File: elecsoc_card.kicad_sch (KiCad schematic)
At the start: 30 parts, among them J1 Conn_01x02_Pin, J2 Conn_01x02_Pin, U1 NA555D

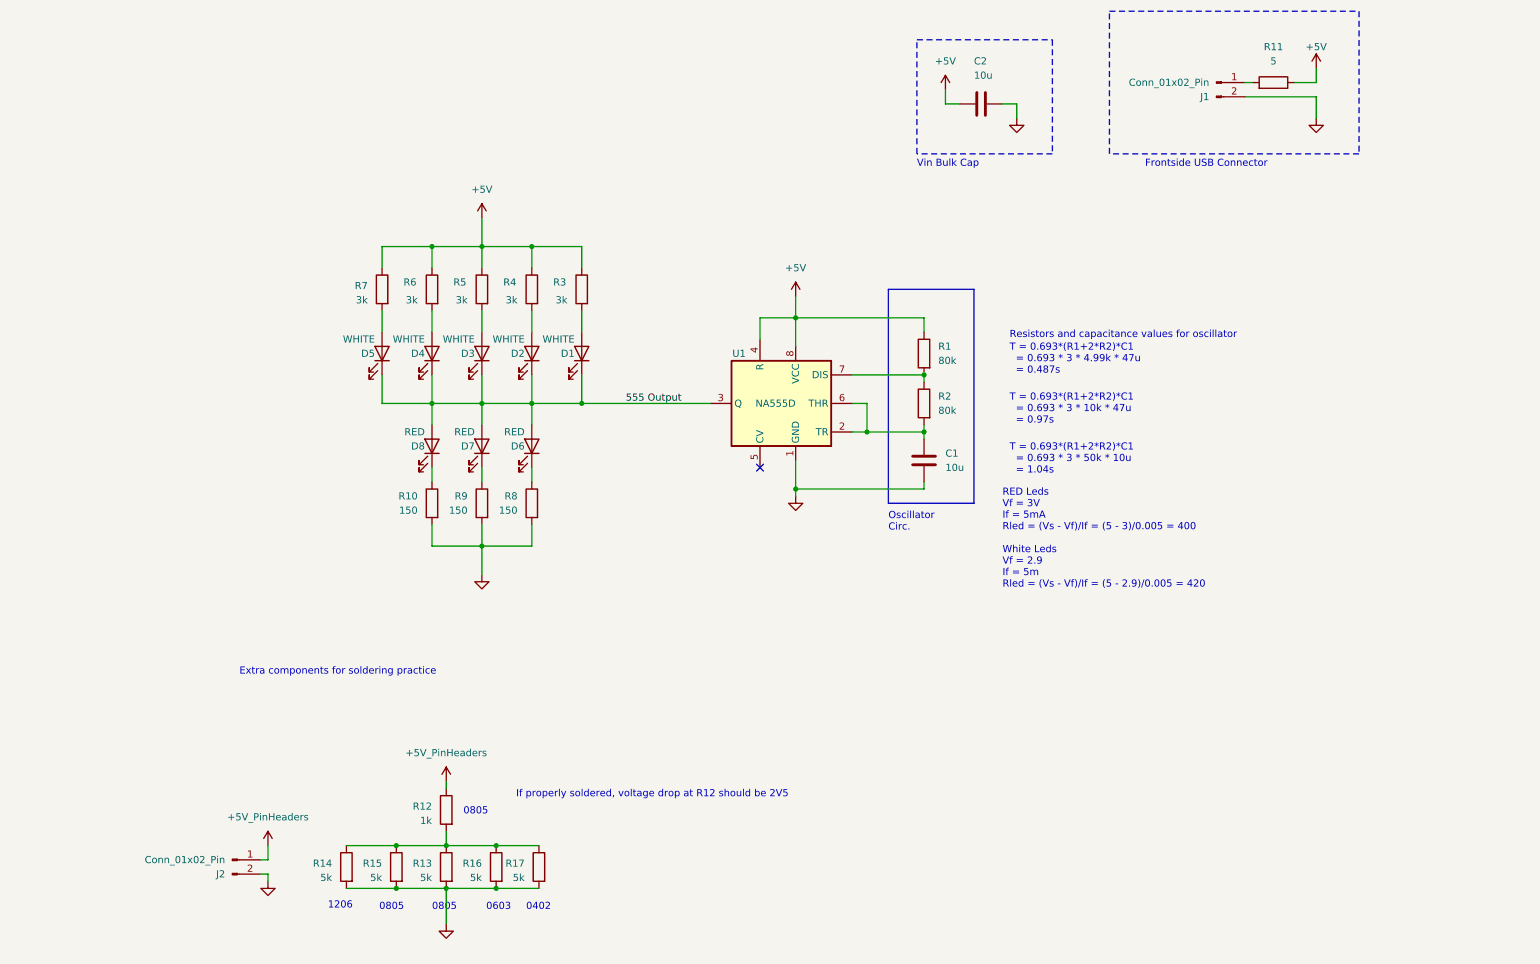
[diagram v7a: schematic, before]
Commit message: Added extra parallel cap to see how the change in capacitance affects the period
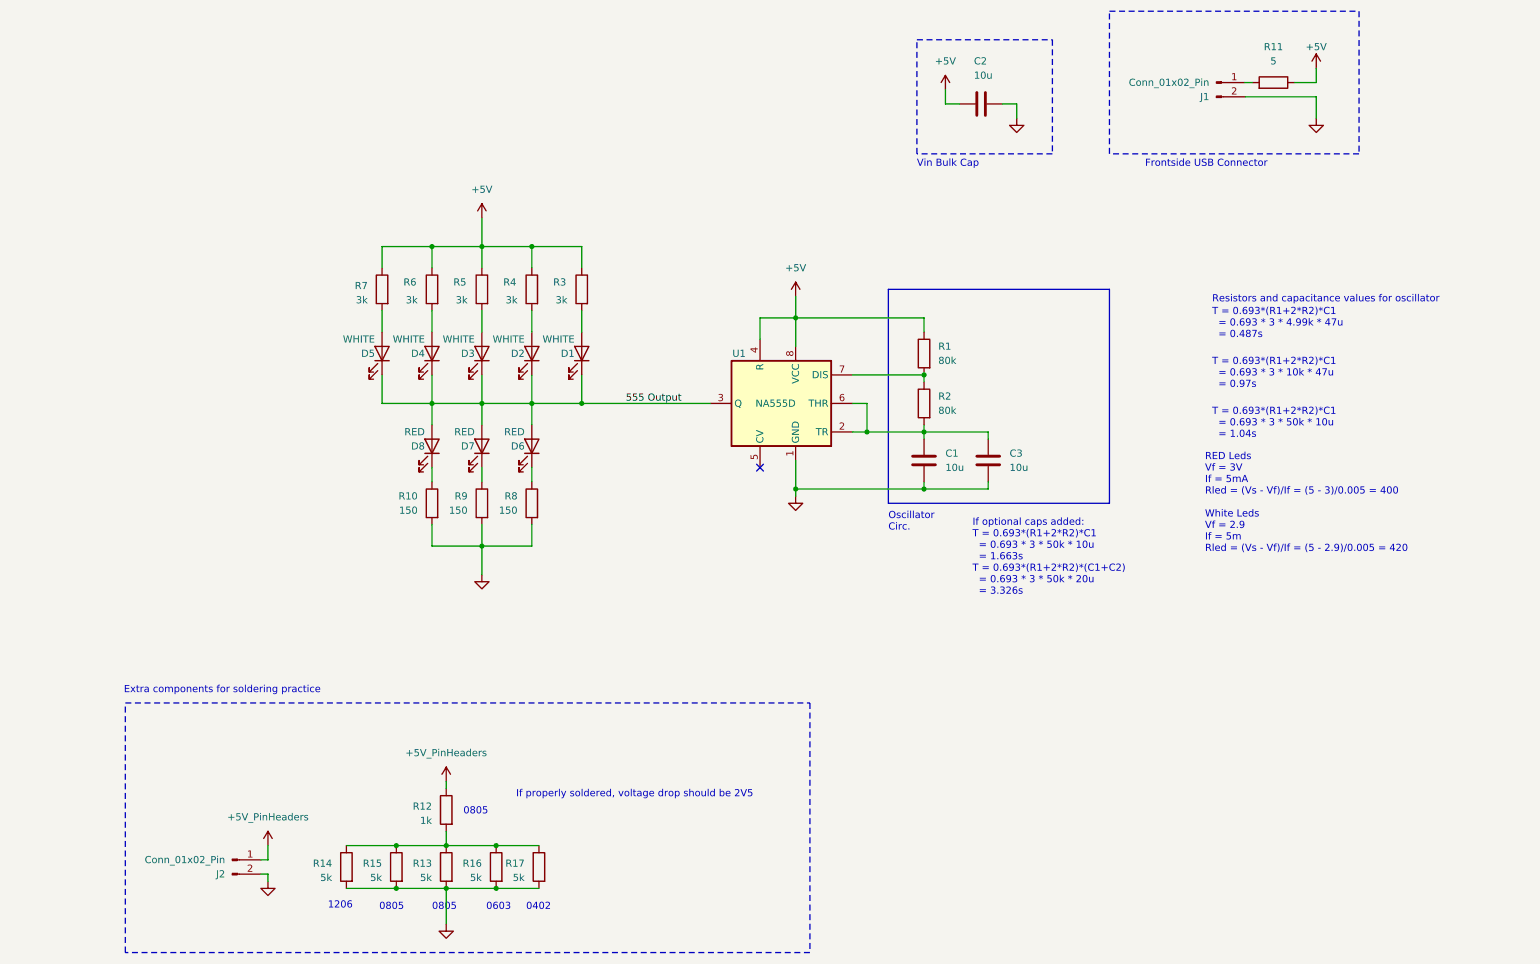
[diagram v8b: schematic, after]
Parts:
- added C3: 10u, Capacitor_SMD:C_0805_2012Metric_Pad1.18x1.45mm_HandSolder, symbol Device:C
- R16: footprint Resistor_SMD:R_0805_2012Metric_Pad1.20x1.40mm_HandSolder -> Resistor_SMD:R_0603_1608Metric
- R17: footprint Resistor_SMD:R_0805_2012Metric_Pad1.20x1.40mm_HandSolder -> Resistor_SMD:R_0402_1005Metric
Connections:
- net GND: now also C3.2
- net at C1.1, R2.2, U1.2 (TR)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: now also C3.1
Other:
- note added: "If optional caps added: T = 0.693*(R1+2*R2)*C1 = 0.693 * 3 * 50k * 10u = 1.663s T = 0.693*(R1+2*R2)*(C1+C2) = 0.693 * 3 * 50k * 20u = 3.326s"
- note added: "If properly soldered, voltage drop should be 2V5"
- note removed: "If properly soldered, voltage drop at R12 should be 2V5"
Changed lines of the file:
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@@
 	)
 	(junction
+		(at 181.61 106.68)
+		(diameter 0)
+		(color 0 0 0 0)
+	)
+	(junction
 		(at 120.65 91.44)
 		(diameter 0)
@@
 	(wire
 		(pts
+			(xy 181.61 96.52) (xy 193.04 96.52)
+		)
+		(stroke
+			(width 0)
+			(type default)
+		)
+	)
+	(wire
+		(pts
 			(xy 63.5 175.26) (xy 64.77 175.26)
 		)
@@
 	(wire
 		(pts
+			(xy 181.61 106.68) (xy 193.04 106.68)
+		)
+		(stroke
+			(width 0)
+			(type default)
+		)
+	)
+	(wire
+		(pts
 			(xy 238.76 36.83) (xy 251.46 36.83)
 		)
@@
 	(wire
 		(pts
+			(xy 193.04 97.79) (xy 193.04 96.52)
+		)
+		(stroke
+			(width 0)
+			(type default)
+		)
+	)
+	(wire
+		(pts
 			(xy 181.61 97.79) (xy 181.61 96.52)
 		)
@@
 	(wire
 		(pts
+			(xy 193.04 105.41) (xy 193.04 106.68)
+		)
+		(stroke
+			(width 0)
+			(type default)
+		)
+	)
+	(wire
+		(pts
 			(xy 111.76 63.5) (xy 102.87 63.5)
 		)
@@
 	)
 	(rectangle
+		(start 39.37 144.78)
+		(end 161.29 189.23)
+		(stroke
+			(width 0)
+			(type dash)
+		)
+		(fill
+			(type none)
+		)
+	)
+	(rectangle
 		(start 180.34 26.67)
 		(end 204.47 46.99)
@@
 	(rectangle
 		(start 175.26 71.12)
-		(end 190.5 109.22)
+		(end 214.63 109.22)
 		(stroke
 			(width 0)
@@
 	(text "RED Leds\nVf = 3V\nIf = 5mA\nRled = (Vs - Vf)/If = (5 - 3)/0.005 = 400\n\nWhite Leds\nVf = 2.9\nIf = 5m\nRled = (Vs - Vf)/If = (5 - 2.9)/0.005 = 420"
 		(exclude_from_sim no)
-		(at 195.58 124.46 0)
+		(at 231.648 118.11 0)
 		(effects
 			(font
@@
 	(text "T = 0.693*(R1+2*R2)*C1\n  = 0.693 * 3 * 50k * 10u \n  = 1.04s"
 		(exclude_from_sim no)
-		(at 196.85 104.14 0)
+		(at 232.918 97.79 0)
 		(effects
 			(font
@@
 		)
 	)
+	(text "If optional caps added:\nT = 0.693*(R1+2*R2)*C1\n  = 0.693 * 3 * 50k * 10u \n  = 1.663s\nT = 0.693*(R1+2*R2)*(C1+C2)\n  = 0.693 * 3 * 50k * 20u \n  = 3.326s"
+		(exclude_from_sim no)
+		(at 190.246 125.73 0)
+		(effects
+			(font
+				(size 1.27 1.27)
+			)
+			(justify left bottom)
+		)
+	)
 	(text "T = 0.693*(R1+2*R2)*C1\n  = 0.693 * 3 * 10k * 47u \n  = 0.97s"
 		(exclude_from_sim no)
-		(at 196.85 95.25 0)
+		(at 232.918 88.9 0)
 		(effects
 			(font
@@
 		)
 	)
-	(text "If properly soldered, voltage drop at R12 should be 2V5\n"
+	(text "If properly soldered, voltage drop should be 2V5\n"
 		(exclude_from_sim no)
 		(at 108.966 161.798 0)
@@
 	(text "Resistors and capacitance values for oscillator"
 		(exclude_from_sim no)
-		(at 196.85 80.01 0)
+		(at 232.918 73.66 0)
 		(effects
 			(font
@@
 	(text "T = 0.693*(R1+2*R2)*C1\n  = 0.693 * 3 * 4.99k * 47u \n  = 0.487s"
 		(exclude_from_sim no)
-		(at 196.85 86.36 0)
+		(at 232.918 80.01 0)
 		(effects
 			(font
@@
 	(text "Extra components for soldering practice\n"
 		(exclude_from_sim no)
-		(at 59.69 139.954 0)
+		(at 39.116 143.256 0)
 		(effects
 			(font
@@
 			)
 		)
-		(property "Footprint" "Resistor_SMD:R_0805_2012Metric_Pad1.20x1.40mm_HandSolder"
+		(property "Footprint" "Resistor_SMD:R_0603_1608Metric"
 			(at 107.188 173.99 90)
 			(effects
@@
 			)
 		)
-		(property "Footprint" "Resistor_SMD:R_0805_2012Metric_Pad1.20x1.40mm_HandSolder"
+		(property "Footprint" "Resistor_SMD:R_0402_1005Metric"
 			(at 114.808 173.99 90)
 			(effects
@@
 					(unit 1)
 				)
+			)
+		)
+	)
+	(symbol
+		(lib_id "Device:C")
+		(at 193.04 101.6 0)
+		(mirror y)
+		(unit 1)
+		(exclude_from_sim no)
+		(in_bom yes)
+		(on_board yes)
+		(dnp no)
+		(property "Reference" "C3"
+			(at 196.85 100.33 0)
+			(effects
+				(font
+					(size 1.27 1.27)
+				)
+				(justify right)
+			)
+		)
+		(property "Value" "10u"
+			(at 196.85 102.87 0)
+			(effects
+				(font
+					(size 1.27 1.27)
+				)
+				(justify right)
+			)
+		)
+		(property "Footprint" "Capacitor_SMD:C_0805_2012Metric_Pad1.18x1.45mm_HandSolder"
+			(at 192.0748 105.41 0)
+			(effects
+				(font
+					(size 1.27 1.27)
+				)
+				(hide yes)
+			)
+		)
+		(property "Datasheet" "https://www.mouser.ie/datasheet/2/281/1/GRT155D70G106ME13_01A-3135786.pdf"
+			(at 193.04 101.6 0)
+			(effects
+				(font
+					(size 1.27 1.27)
+				)
+				(hide yes)
+			)
+		)
+		(property "Description" ""
+			(at 193.04 101.6 0)
+			(effects
+				(font
+					(size 1.27 1.27)
+				)
+				(hide yes)
+			)
+		)
+		(pin "1"
+		)
+		(pin "2"
+		)
+		(instances
+			(project "elecsoc_card"
+				(path "/ec1e128b-e85b-4f54-a1e1-536be465431f"
+					(reference "C3")
+					(unit 1)
+				)
